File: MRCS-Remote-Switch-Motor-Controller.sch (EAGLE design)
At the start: 13 parts, among them CON1 CONNECTOR-M03350-LOCK, J1 J1, J2 J2, M1 WIREPAD2,54/1,1, M8 WIREPAD2,54/1,1, Q1 2N3904, U1 TC4428A

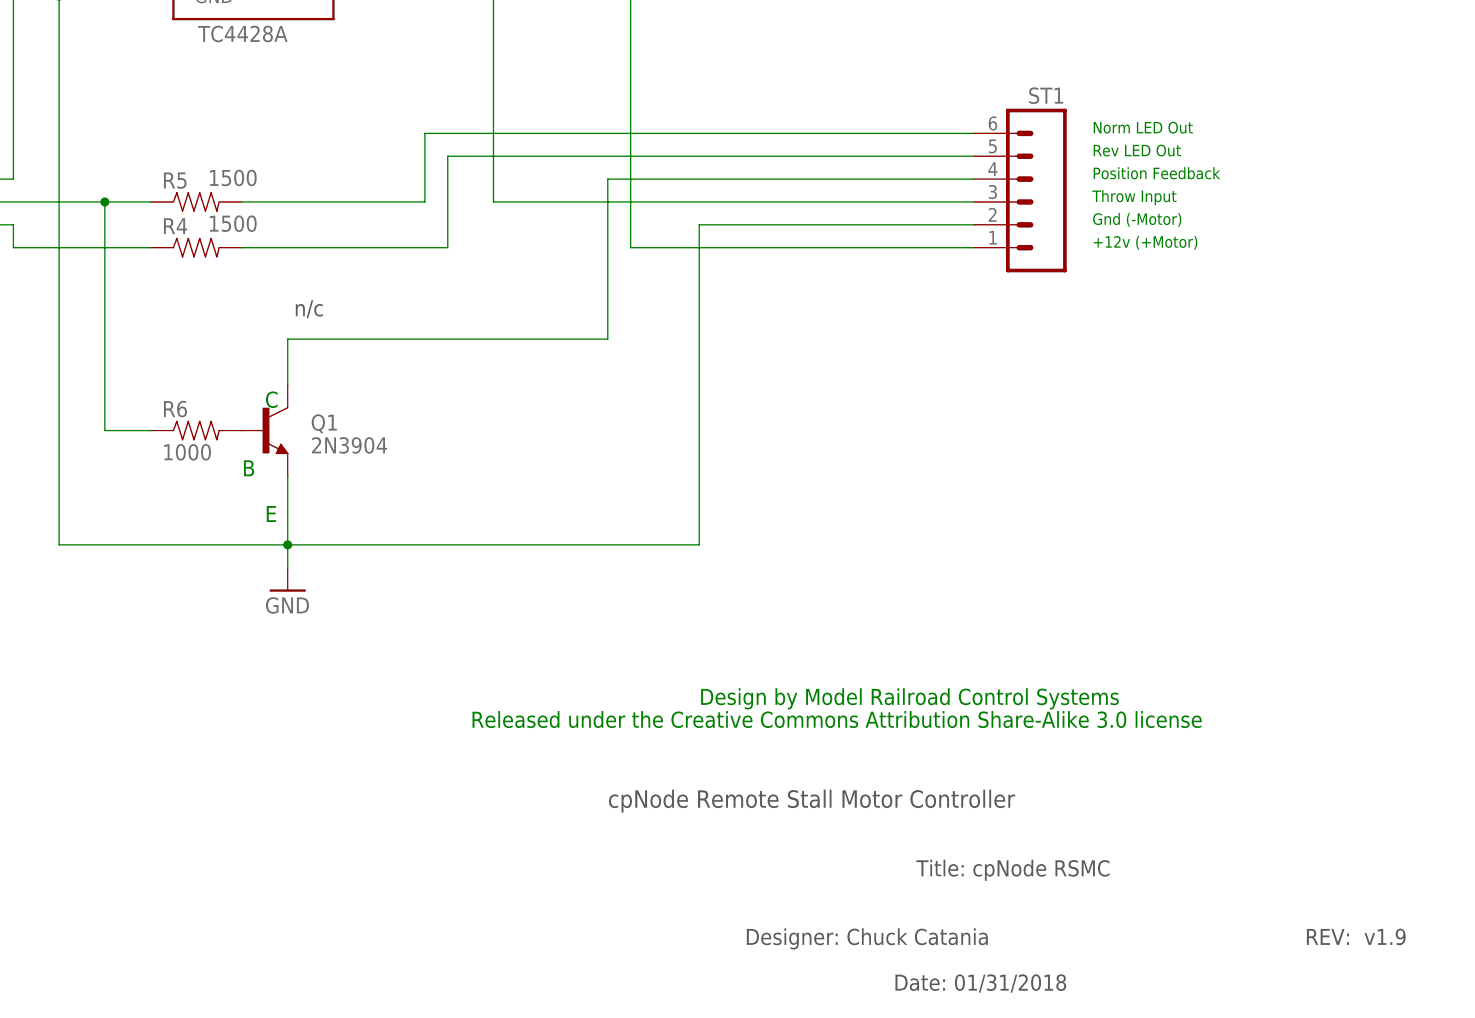
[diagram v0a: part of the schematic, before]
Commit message: Added work files to gitignore and label changes
Added work files to gitignore and made labels on board 56 mil rather than 32 so they can be read more easily
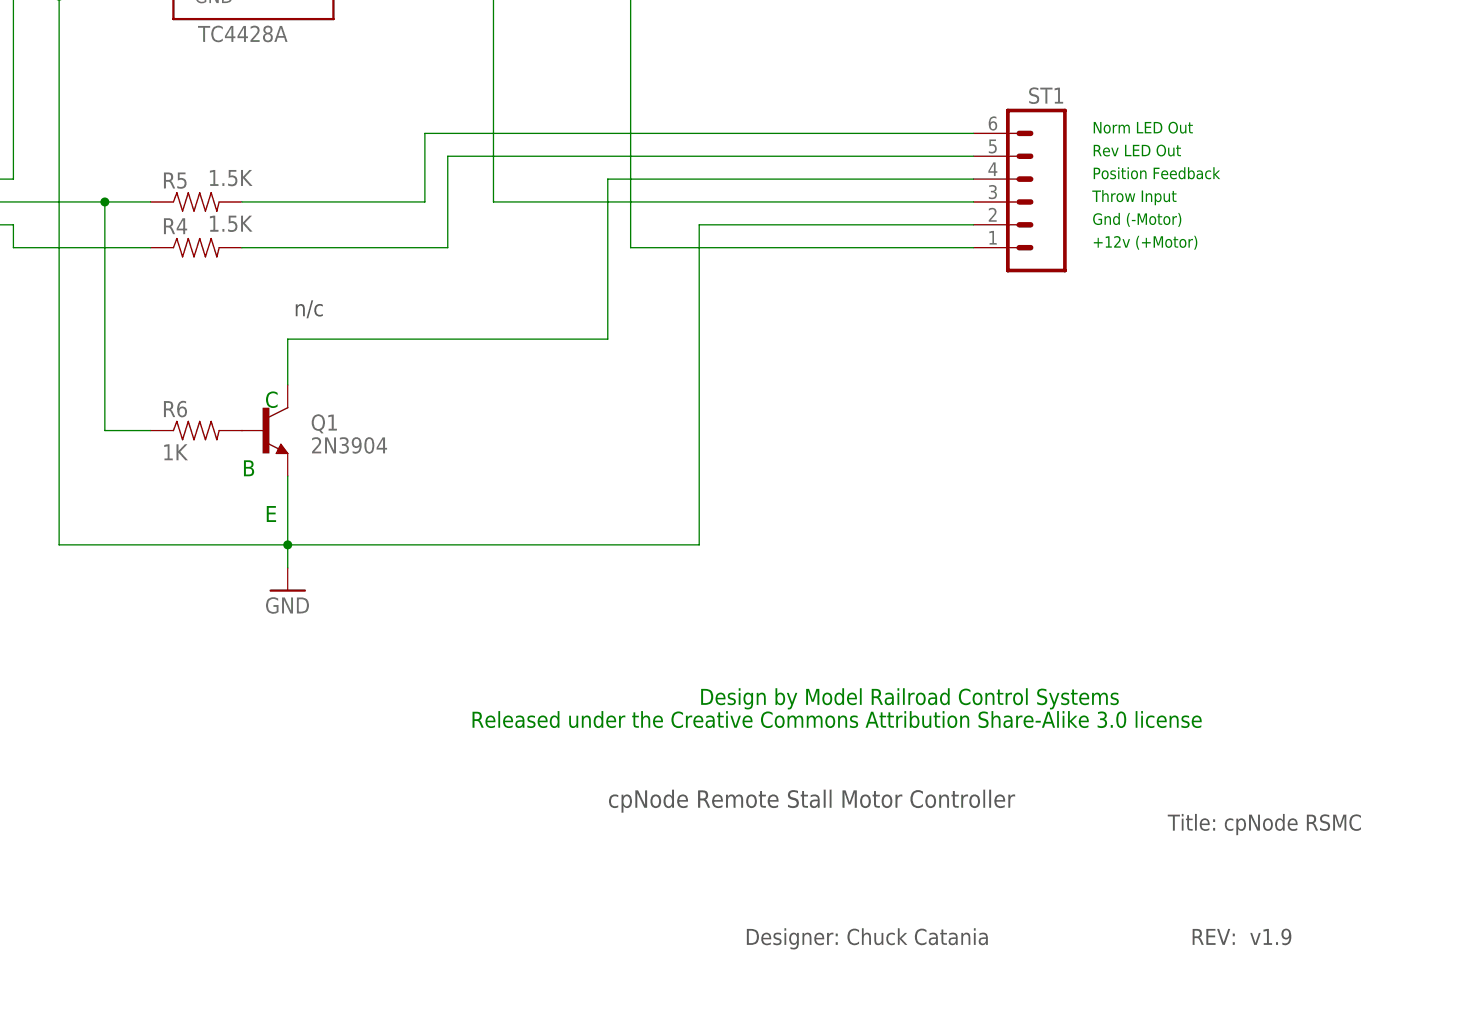
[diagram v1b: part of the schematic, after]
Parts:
- R4, R5: value 1500 -> 1.5K
- R6: value 1000 -> 1K
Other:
- note removed: "Date: 01/31/2018"
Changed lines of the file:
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@@
 <grid distance="100" unitdist="mil" unit="mil" style="dots" multiple="1" display="yes" altdistance="50" altunitdist="mil" altunit="mil"/>
 <layers>
-<layer number="1" name="Top" color="4" fill="1" visible="yes" active="no"/>
-<layer number="2" name="Route2" color="1" fill="3" visible="yes" active="no"/>
-<layer number="3" name="Route3" color="4" fill="3" visible="yes" active="no"/>
-<layer number="14" name="Route14" color="1" fill="6" visible="yes" active="no"/>
-<layer number="15" name="Route15" color="4" fill="6" visible="yes" active="no"/>
-<layer number="16" name="Bottom" color="1" fill="1" visible="yes" active="no"/>
-<layer number="17" name="Pads" color="2" fill="1" visible="yes" active="no"/>
-<layer number="18" name="Vias" color="2" fill="1" visible="yes" active="no"/>
-<layer number="19" name="Unrouted" color="6" fill="1" visible="yes" active="no"/>
-<layer number="20" name="Dimension" color="15" fill="1" visible="yes" active="no"/>
-<layer number="21" name="tPlace" color="7" fill="1" visible="yes" active="no"/>
-<layer number="22" name="bPlace" color="7" fill="1" visible="yes" active="no"/>
-<layer number="23" name="tOrigins" color="15" fill="1" visible="yes" active="no"/>
-<layer number="24" name="bOrigins" color="15" fill="1" visible="yes" active="no"/>
-<layer number="25" name="tNames" color="7" fill="1" visible="yes" active="no"/>
-<layer number="26" name="bNames" color="7" fill="1" visible="yes" active="no"/>
-<layer number="27" name="tValues" color="7" fill="1" visible="yes" active="no"/>
-<layer number="28" name="bValues" color="7" fill="1" visible="yes" active="no"/>
+<layer number="1" name="Top" color="4" fill="1" visible="no" active="no"/>
+<layer number="2" name="Route2" color="1" fill="3" visible="no" active="no"/>
+<layer number="3" name="Route3" color="4" fill="3" visible="no" active="no"/>
+<layer number="14" name="Route14" color="1" fill="6" visible="no" active="no"/>
+<layer number="15" name="Route15" color="4" fill="6" visible="no" active="no"/>
+<layer number="16" name="Bottom" color="1" fill="1" visible="no" active="no"/>
+<layer number="17" name="Pads" color="2" fill="1" visible="no" active="no"/>
+<layer number="18" name="Vias" color="2" fill="1" visible="no" active="no"/>
+<layer number="19" name="Unrouted" color="6" fill="1" visible="no" active="no"/>
+<layer number="20" name="Dimension" color="15" fill="1" visible="no" active="no"/>
+<layer number="21" name="tPlace" color="7" fill="1" visible="no" active="no"/>
+<layer number="22" name="bPlace" color="7" fill="1" visible="no" active="no"/>
+<layer number="23" name="tOrigins" color="15" fill="1" visible="no" active="no"/>
+<layer number="24" name="bOrigins" color="15" fill="1" visible="no" active="no"/>
+<layer number="25" name="tNames" color="7" fill="1" visible="no" active="no"/>
+<layer number="26" name="bNames" color="7" fill="1" visible="no" active="no"/>
+<layer number="27" name="tValues" color="7" fill="1" visible="no" active="no"/>
+<layer number="28" name="bValues" color="7" fill="1" visible="no" active="no"/>
 <layer number="29" name="tStop" color="7" fill="3" visible="no" active="no"/>
 <layer number="30" name="bStop" color="7" fill="6" visible="no" active="no"/>
@@
 <layer number="35" name="tGlue" color="7" fill="4" visible="no" active="no"/>
 <layer number="36" name="bGlue" color="7" fill="5" visible="no" active="no"/>
-<layer number="37" name="tTest" color="7" fill="1" visible="yes" active="no"/>
-<layer number="38" name="bTest" color="7" fill="1" visible="yes" active="no"/>
+<layer number="37" name="tTest" color="7" fill="1" visible="no" active="no"/>
+<layer number="38" name="bTest" color="7" fill="1" visible="no" active="no"/>
 <layer number="39" name="tKeepout" color="4" fill="11" visible="no" active="no"/>
 <layer number="40" name="bKeepout" color="1" fill="11" visible="no" active="no"/>
@@
 <layer number="44" name="Drills" color="7" fill="1" visible="no" active="no"/>
 <layer number="45" name="Holes" color="7" fill="1" visible="no" active="no"/>
-<layer number="46" name="Milling" color="3" fill="1" visible="yes" active="no"/>
-<layer number="47" name="Measures" color="7" fill="1" visible="yes" active="no"/>
-<layer number="48" name="Document" color="7" fill="1" visible="yes" active="no"/>
-<layer number="49" name="Reference" color="7" fill="1" visible="yes" active="no"/>
-<layer number="50" name="dxf" color="7" fill="1" visible="yes" active="no"/>
-<layer number="51" name="tDocu" color="7" fill="1" visible="yes" active="no"/>
-<layer number="52" name="bDocu" color="7" fill="1" visible="yes" active="no"/>
-<layer number="53" name="tGND_GNDA" color="7" fill="9" visible="yes" active="no"/>
-<layer number="54" name="bGND_GNDA" color="1" fill="9" visible="yes" active="no"/>
-<layer number="56" name="wert" color="7" fill="1" visible="yes" active="no"/>
-<layer number="57" name="tCAD" color="7" fill="1" visible="yes" active="no"/>
-<layer number="59" name="tCarbon" color="7" fill="1" visible="yes" active="no"/>
-<layer number="60" name="bCarbon" color="7" fill="1" visible="yes" active="no"/>
+<layer number="46" name="Milling" color="3" fill="1" visible="no" active="no"/>
+<layer number="47" name="Measures" color="7" fill="1" visible="no" active="no"/>
+<layer number="48" name="Document" color="7" fill="1" visible="no" active="no"/>
+<layer number="49" name="Reference" color="7" fill="1" visible="no" active="no"/>
+<layer number="50" name="dxf" color="7" fill="1" visible="no" active="no"/>
+<layer number="51" name="tDocu" color="7" fill="1" visible="no" active="no"/>
+<layer number="52" name="bDocu" color="7" fill="1" visible="no" active="no"/>
+<layer number="53" name="tGND_GNDA" color="7" fill="9" visible="no" active="no"/>
+<layer number="54" name="bGND_GNDA" color="1" fill="9" visible="no" active="no"/>
+<layer number="56" name="wert" color="7" fill="1" visible="no" active="no"/>
+<layer number="57" name="tCAD" color="7" fill="1" visible="no" active="no"/>
+<layer number="59" name="tCarbon" color="7" fill="1" visible="no" active="no"/>
+<layer number="60" name="bCarbon" color="7" fill="1" visible="no" active="no"/>
 <layer number="90" name="Modules" color="5" fill="1" visible="yes" active="yes"/>
 <layer number="91" name="Nets" color="2" fill="1" visible="yes" active="yes"/>
@@
 </classes>
 <parts>
-<part name="R5" library="SPCoast" deviceset="R*" device="PTH04" value="1500"/>
-<part name="R4" library="SPCoast" deviceset="R*" device="PTH04" value="1500"/>
+<part name="R5" library="SPCoast" deviceset="R*" device="PTH04" value="1.5K"/>
+<part name="R4" library="SPCoast" deviceset="R*" device="PTH04" value="1.5K"/>
 <part name="ST1" library="SparkFun-Connectors" deviceset="M06" device="LOCK"/>
 <part name="Q1" library="SPCoast" deviceset="NPN" device="-MS-013" value="2N3904"/>
 <part name="C1" library="SparkFun-Capacitors" deviceset="CAP" device="EZ" value=".01uF"/>
 <part name="R3" library="SPCoast" deviceset="R*" device="PTH04" value="1M"/>
-<part name="R6" library="SPCoast" deviceset="R*" device="PTH04" value="1000"/>
+<part name="R6" library="SPCoast" deviceset="R*" device="PTH04" value="1K"/>
 <part name="U1" library="ir" deviceset="IR4428" device="" value="TC4428A"/>
 <part name="J2" library="SparkFun-Connectors" deviceset="M08" device="" value="J2"/>
@@
 <text x="111.76" y="63.5" size="1.778" layer="91">C</text>
 <text x="149.86" y="19.05" size="1.9304" layer="97">cpNode Remote Stall Motor Controller</text>
-<text x="184.15" y="11.43" size="1.778" layer="97" font="vector">Title: cpNode RSMC</text>
-<text x="181.61" y="-1.27" size="1.778" layer="97" font="vector">Date: 01/31/2018</text>
+<text x="212.09" y="16.51" size="1.778" layer="97" font="vector">Title: cpNode RSMC</text>
 <text x="165.1" y="3.81" size="1.778" layer="97">Designer: Chuck Catania</text>
-<text x="227.33" y="3.81" size="1.778" layer="97" font="vector">REV:  v1.9</text>
+<text x="214.63" y="3.81" size="1.778" layer="97" font="vector">REV:  v1.9</text>
 <text x="114.3" y="73.66" size="1.778" layer="97" font="vector"> n/c</text>
 <text x="2.54" y="25.4" size="1.6764" layer="97">Special Thanks to:</text>

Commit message: Updated Documentation and created pdf
documentation
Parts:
- C1: device SparkFun-Capacitors:CAPEZ -> SparkFun-Passives:CAPEZ
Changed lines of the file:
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@@
 <part name="ST1" library="SparkFun-Connectors" deviceset="M06" device="LOCK"/>
 <part name="Q1" library="SPCoast" deviceset="NPN" device="-MS-013" value="2N3904"/>
-<part name="C1" library="SparkFun-Capacitors" deviceset="CAP" device="EZ" value=".01uF"/>
+<part name="C1" library="SparkFun-Passives" deviceset="CAP" device="EZ" value=".01uF"/>
 <part name="R3" library="SPCoast" deviceset="R*" device="PTH04" value="1M"/>
 <part name="R6" library="SPCoast" deviceset="R*" device="PTH04" value="1K"/>
